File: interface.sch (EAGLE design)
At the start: 23 parts, among them U1 ISL3179EIBZ, U2 ATMEGA328P

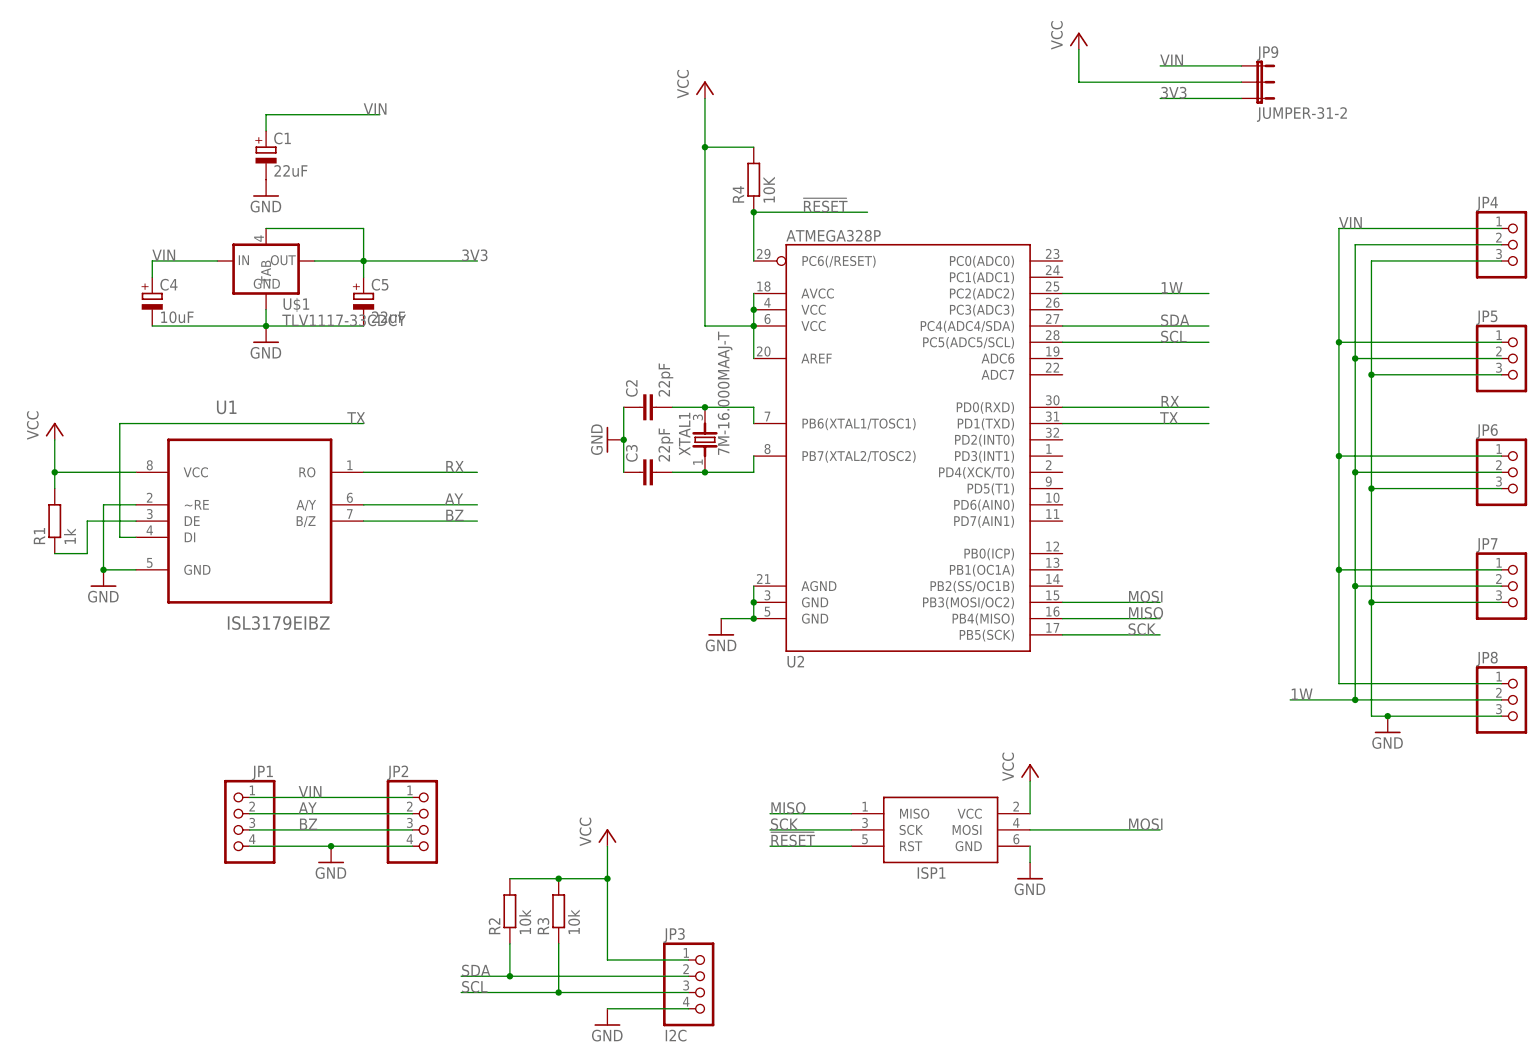
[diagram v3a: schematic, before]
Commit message: now has 2 I2C busses
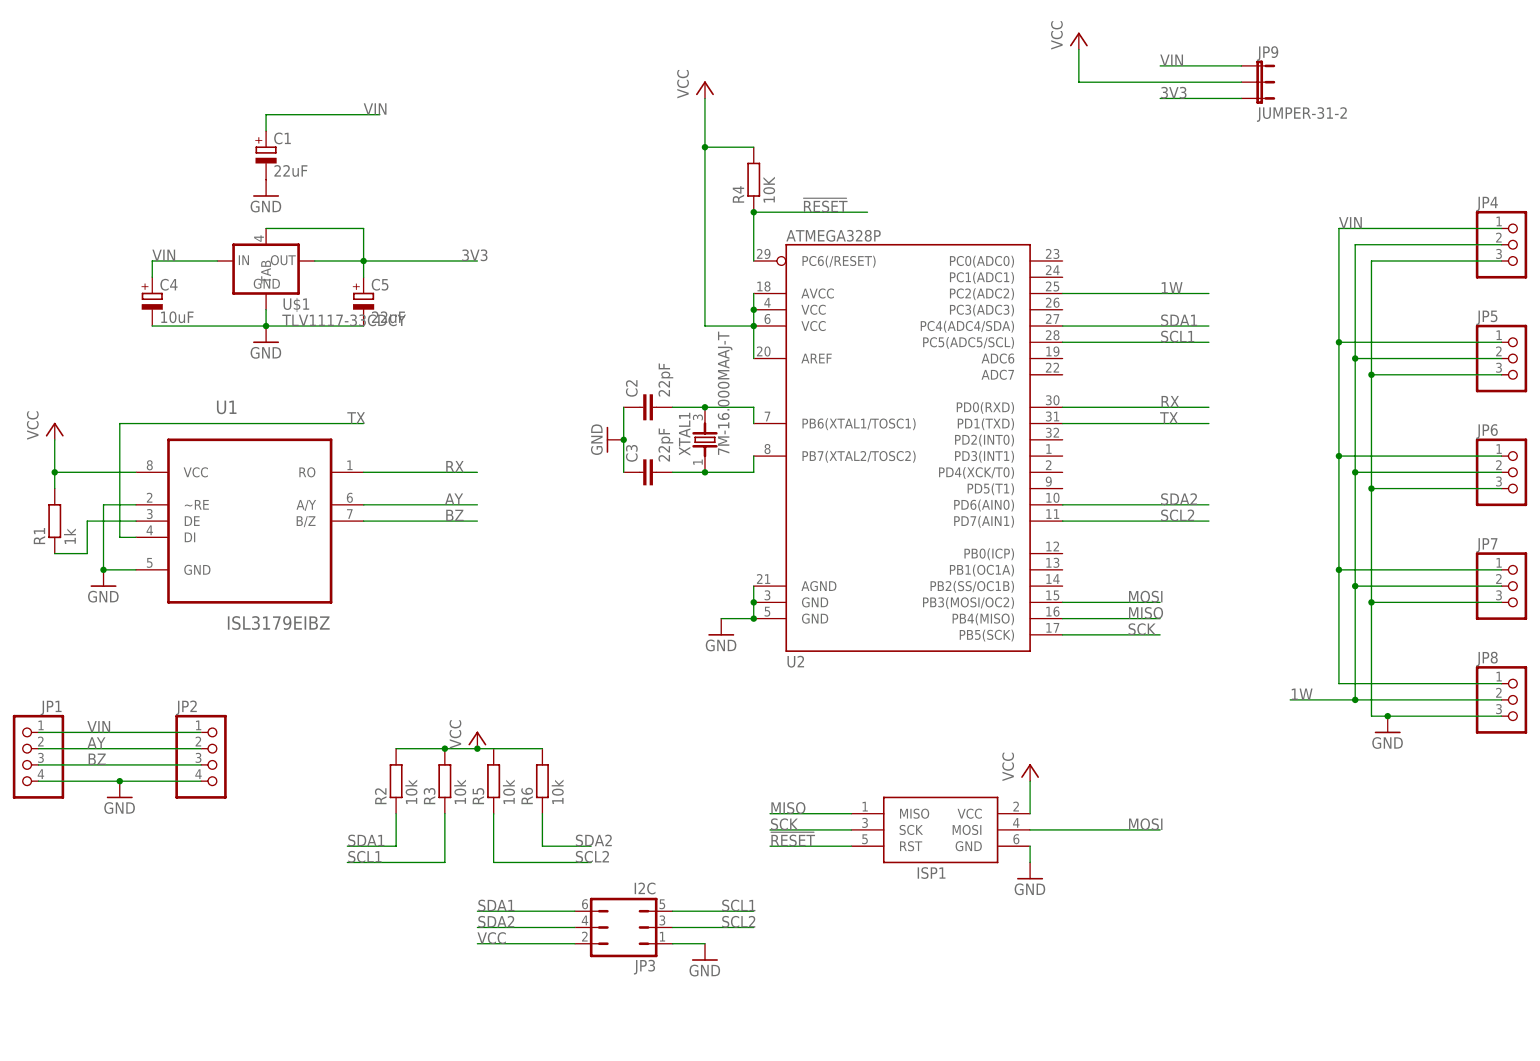
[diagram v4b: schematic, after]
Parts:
- added R5, R6: 10k, resistor:R-EU_R0805
- JP3: device pinhead:PINHD-1X4 -> jumper:JP3Q
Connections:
- removed net SCL: JP3.3, R3.1, U2.PC5(ADC5/SCL)
- removed net SDA: JP3.2, R2.1, U2.PC4(ADC4/SDA)
- new net SCL1: JP3.5, R3.1, U2.PC5(ADC5/SCL)
- new net SCL2: JP3.3, R5.1, U2.PD7(AIN1)
- new net SDA1: JP3.6, R2.1, U2.PC4(ADC4/SDA)
- new net SDA2: JP3.4, R6.1, U2.PD6(AIN0)
- net GND: now also JP3.1; no longer JP3.4
- net VCC: now also JP3.2, R5.2, R6.2; no longer JP3.1
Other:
- moved on the sheet: JP1, JP2, R2, R3
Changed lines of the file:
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@@
 <part name="GND1" library="supply1" deviceset="GND" device=""/>
 <part name="P+4" library="glacsweb" deviceset="VCC" device=""/>
-<part name="JP3" library="pinhead" deviceset="PINHD-1X4" device="" value="I2C"/>
+<part name="JP3" library="jumper" deviceset="JP3Q" device="" value="I2C"/>
 <part name="GND2" library="supply1" deviceset="GND" device=""/>
 <part name="P+6" library="glacsweb" deviceset="VCC" device=""/>
@@
 <part name="JP9" library="SparkFun-Passives" deviceset="JUMPER-3" device="1-2"/>
 <part name="P+5" library="glacsweb" deviceset="VCC" device=""/>
+<part name="R5" library="resistor" deviceset="R-EU_" device="R0805" value="10k"/>
+<part name="R6" library="resistor" deviceset="R-EU_" device="R0805" value="10k"/>
 </parts>
 <sheets>
@@
 <instance part="P+2" gate="VCC" x="165.1" y="53.34"/>
 <instance part="GND5" gate="1" x="165.1" y="35.56"/>
-<instance part="JP2" gate="A" x="71.12" y="43.18"/>
-<instance part="JP1" gate="A" x="40.64" y="43.18" rot="MR0"/>
-<instance part="GND6" gate="1" x="55.88" y="38.1"/>
+<instance part="JP2" gate="A" x="38.1" y="53.34"/>
+<instance part="JP1" gate="A" x="7.62" y="53.34" rot="MR0"/>
+<instance part="GND6" gate="1" x="22.86" y="48.26"/>
 <instance part="GND1" gate="1" x="45.72" y="142.24"/>
 <instance part="P+4" gate="VCC" x="12.7" y="106.68"/>
-<instance part="JP3" gate="A" x="114.3" y="17.78"/>
-<instance part="GND2" gate="1" x="99.06" y="12.7"/>
-<instance part="P+6" gate="VCC" x="99.06" y="43.18"/>
+<instance part="JP3" gate="B" x="101.6" y="27.94" rot="R90"/>
+<instance part="GND2" gate="1" x="114.3" y="22.86"/>
+<instance part="P+6" gate="VCC" x="78.74" y="58.42"/>
 <instance part="JP4" gate="A" x="241.3" y="134.62"/>
 <instance part="JP5" gate="A" x="241.3" y="116.84"/>
@@
 <instance part="JP8" gate="A" x="241.3" y="63.5"/>
 <instance part="GND7" gate="1" x="220.98" y="58.42"/>
-<instance part="R3" gate="G$1" x="91.44" y="30.48" rot="R90"/>
-<instance part="R2" gate="G$1" x="83.82" y="30.48" rot="R90"/>
+<instance part="R3" gate="G$1" x="73.66" y="50.8" rot="R90"/>
+<instance part="R2" gate="G$1" x="66.04" y="50.8" rot="R90"/>
 <instance part="U2" gate="G$1" x="144.78" y="106.68"/>
 <instance part="GND8" gate="1" x="116.84" y="73.66"/>
@@
 <instance part="JP9" gate="G$1" x="200.66" y="162.56" rot="R270"/>
 <instance part="P+5" gate="VCC" x="172.72" y="167.64"/>
+<instance part="R5" gate="G$1" x="81.28" y="50.8" rot="R90"/>
+<instance part="R6" gate="G$1" x="88.9" y="50.8" rot="R90"/>
 </instances>
 <busses>
@@
 <pinref part="JP1" gate="A" pin="4"/>
 <pinref part="JP2" gate="A" pin="4"/>
-<wire x1="43.18" y1="40.64" x2="55.88" y2="40.64" width="0.1524" layer="91"/>
+<wire x1="10.16" y1="50.8" x2="22.86" y2="50.8" width="0.1524" layer="91"/>
 <pinref part="GND6" gate="1" pin="GND"/>
-<wire x1="55.88" y1="40.64" x2="68.58" y2="40.64" width="0.1524" layer="91"/>
-<junction x="55.88" y="40.64"/>
+<wire x1="22.86" y1="50.8" x2="35.56" y2="50.8" width="0.1524" layer="91"/>
+<junction x="22.86" y="50.8"/>
 </segment>
 <segment>
 <pinref part="C1" gate="G$1" pin="-"/>
 <pinref part="GND1" gate="1" pin="GND"/>
-</segment>
-<segment>
-<pinref part="JP3" gate="A" pin="4"/>
-<pinref part="GND2" gate="1" pin="GND"/>
-<wire x1="111.76" y1="15.24" x2="99.06" y2="15.24" width="0.1524" layer="91"/>
 </segment>
 <segment>
@@
 <pinref part="GND9" gate="1" pin="GND"/>
 </segment>
+<segment>
+<pinref part="JP3" gate="B" pin="1"/>
+<pinref part="GND2" gate="1" pin="GND"/>
+<wire x1="109.22" y1="25.4" x2="114.3" y2="25.4" width="0.1524" layer="91"/>
+</segment>
 </net>
 <net name="VCC" class="0">
@@
 <wire x1="12.7" y1="96.52" x2="12.7" y2="99.06" width="0.1524" layer="91"/>
 <junction x="12.7" y="99.06"/>
-</segment>
-<segment>
-<pinref part="JP3" gate="A" pin="1"/>
-<pinref part="P+6" gate="VCC" pin="VCC"/>
-<wire x1="111.76" y1="22.86" x2="99.06" y2="22.86" width="0.1524" layer="91"/>
-<wire x1="99.06" y1="22.86" x2="99.06" y2="35.56" width="0.1524" layer="91"/>
-<pinref part="R2" gate="G$1" pin="2"/>
-<wire x1="99.06" y1="35.56" x2="99.06" y2="40.64" width="0.1524" layer="91"/>
-<wire x1="83.82" y1="35.56" x2="91.44" y2="35.56" width="0.1524" layer="91"/>
-<pinref part="R3" gate="G$1" pin="2"/>
-<junction x="91.44" y="35.56"/>
-<wire x1="91.44" y1="35.56" x2="99.06" y2="35.56" width="0.1524" layer="91"/>
-<junction x="99.06" y="35.56"/>
 </segment>
 <segment>
@@
 <pinref part="P+5" gate="VCC" pin="VCC"/>
 </segment>
+<segment>
+<pinref part="JP3" gate="B" pin="2"/>
+<wire x1="93.98" y1="25.4" x2="78.74" y2="25.4" width="0.1524" layer="91"/>
+<label x="78.74" y="25.4" size="1.778" layer="95"/>
+</segment>
+<segment>
+<pinref part="R2" gate="G$1" pin="2"/>
+<wire x1="66.04" y1="55.88" x2="73.66" y2="55.88" width="0.1524" layer="91"/>
+<pinref part="R3" gate="G$1" pin="2"/>
+<junction x="73.66" y="55.88"/>
+<wire x1="73.66" y1="55.88" x2="78.74" y2="55.88" width="0.1524" layer="91"/>
+<pinref part="R5" gate="G$1" pin="2"/>
+<pinref part="R6" gate="G$1" pin="2"/>
+<wire x1="78.74" y1="55.88" x2="81.28" y2="55.88" width="0.1524" layer="91"/>
+<wire x1="88.9" y1="55.88" x2="81.28" y2="55.88" width="0.1524" layer="91"/>
+<pinref part="P+6" gate="VCC" pin="VCC"/>
+<junction x="78.74" y="55.88"/>
+</segment>
 </net>
 <net name="AY" class="0">
@@
 <pinref part="JP2" gate="A" pin="2"/>
 <pinref part="JP1" gate="A" pin="2"/>
-<wire x1="68.58" y1="45.72" x2="43.18" y2="45.72" width="0.1524" layer="91"/>
-<label x="50.8" y="45.72" size="1.778" layer="95"/>
+<wire x1="35.56" y1="55.88" x2="10.16" y2="55.88" width="0.1524" layer="91"/>
+<label x="17.78" y="55.88" size="1.778" layer="95"/>
 </segment>
 </net>
@@
 <pinref part="JP1" gate="A" pin="3"/>
 <pinref part="JP2" gate="A" pin="3"/>
-<wire x1="43.18" y1="43.18" x2="68.58" y2="43.18" width="0.1524" layer="91"/>
-<label x="50.8" y="43.18" size="1.778" layer="95"/>
+<wire x1="10.16" y1="53.34" x2="35.56" y2="53.34" width="0.1524" layer="91"/>
+<label x="17.78" y="53.34" size="1.778" layer="95"/>
 </segment>
 </net>
@@
 </segment>
 </net>
-<net name="SDA" class="0">
-<segment>
-<pinref part="JP3" gate="A" pin="2"/>
-<wire x1="111.76" y1="20.32" x2="83.82" y2="20.32" width="0.1524" layer="91"/>
-<label x="76.2" y="20.32" size="1.778" layer="95"/>
+<net name="SDA1" class="0">
+<segment>
+<label x="58.42" y="40.64" size="1.778" layer="95"/>
 <pinref part="R2" gate="G$1" pin="1"/>
-<wire x1="83.82" y1="20.32" x2="76.2" y2="20.32" width="0.1524" layer="91"/>
-<wire x1="83.82" y1="25.4" x2="83.82" y2="20.32" width="0.1524" layer="91"/>
-<junction x="83.82" y="20.32"/>
+<wire x1="66.04" y1="40.64" x2="58.42" y2="40.64" width="0.1524" layer="91"/>
+<wire x1="66.04" y1="45.72" x2="66.04" y2="40.64" width="0.1524" layer="91"/>
 </segment>
 <segment>
@@
 <label x="185.42" y="121.92" size="1.778" layer="95"/>
 </segment>
-</net>
-<net name="SCL" class="0">
-<segment>
-<pinref part="JP3" gate="A" pin="3"/>
-<wire x1="111.76" y1="17.78" x2="91.44" y2="17.78" width="0.1524" layer="91"/>
-<label x="76.2" y="17.78" size="1.778" layer="95"/>
+<segment>
+<pinref part="JP3" gate="B" pin="6"/>
+<wire x1="93.98" y1="30.48" x2="78.74" y2="30.48" width="0.1524" layer="91"/>
+<label x="78.74" y="30.48" size="1.778" layer="95"/>
+</segment>
+</net>
+<net name="SCL1" class="0">
+<segment>
+<label x="58.42" y="38.1" size="1.778" layer="95"/>
 <pinref part="R3" gate="G$1" pin="1"/>
-<wire x1="91.44" y1="17.78" x2="76.2" y2="17.78" width="0.1524" layer="91"/>
-<wire x1="91.44" y1="25.4" x2="91.44" y2="17.78" width="0.1524" layer="91"/>
-<junction x="91.44" y="17.78"/>
+<wire x1="73.66" y1="38.1" x2="58.42" y2="38.1" width="0.1524" layer="91"/>
+<wire x1="73.66" y1="45.72" x2="73.66" y2="38.1" width="0.1524" layer="91"/>
 </segment>
 <segment>
@@
 <wire x1="170.18" y1="119.38" x2="193.04" y2="119.38" width="0.1524" layer="91"/>
 <label x="185.42" y="119.38" size="1.778" layer="95"/>
+</segment>
+<segment>
+<pinref part="JP3" gate="B" pin="5"/>
+<wire x1="109.22" y1="30.48" x2="121.92" y2="30.48" width="0.1524" layer="91"/>
+<label x="116.84" y="30.48" size="1.778" layer="95"/>
 </segment>
 </net>
@@
 <pinref part="JP1" gate="A" pin="1"/>
 <pinref part="JP2" gate="A" pin="1"/>
-<wire x1="43.18" y1="48.26" x2="68.58" y2="48.26" width="0.1524" layer="91"/>
-<label x="50.8" y="48.26" size="1.778" layer="95"/>
+<wire x1="10.16" y1="58.42" x2="35.56" y2="58.42" width="0.1524" layer="91"/>
+<label x="17.78" y="58.42" size="1.778" layer="95"/>
 </segment>
 <segment>
@@
 </segment>
 </net>
+<net name="SDA2" class="0">
+<segment>
+<pinref part="U2" gate="G$1" pin="PD6(AIN0)"/>
+<wire x1="170.18" y1="93.98" x2="193.04" y2="93.98" width="0.1524" layer="91"/>
+<label x="185.42" y="93.98" size="1.778" layer="95"/>
+</segment>
+<segment>
+<pinref part="R6" gate="G$1" pin="1"/>
+<wire x1="88.9" y1="45.72" x2="88.9" y2="40.64" width="0.1524" layer="91"/>
+<wire x1="88.9" y1="40.64" x2="96.52" y2="40.64" width="0.1524" layer="91"/>
+<label x="93.98" y="40.64" size="1.778" layer="95"/>
+</segment>
+<segment>
+<pinref part="JP3" gate="B" pin="4"/>
+<wire x1="93.98" y1="27.94" x2="78.74" y2="27.94" width="0.1524" layer="91"/>
+<label x="78.74" y="27.94" size="1.778" layer="95"/>
+</segment>
+</net>
+<net name="SCL2" class="0">
+<segment>
+<pinref part="U2" gate="G$1" pin="PD7(AIN1)"/>
+<wire x1="170.18" y1="91.44" x2="193.04" y2="91.44" width="0.1524" layer="91"/>
+<label x="185.42" y="91.44" size="1.778" layer="95"/>
+</segment>
+<segment>
+<pinref part="R5" gate="G$1" pin="1"/>
+<wire x1="81.28" y1="45.72" x2="81.28" y2="38.1" width="0.1524" layer="91"/>
+<wire x1="81.28" y1="38.1" x2="96.52" y2="38.1" width="0.1524" layer="91"/>
+<label x="93.98" y="38.1" size="1.778" layer="95"/>
+</segment>
+<segment>
+<pinref part="JP3" gate="B" pin="3"/>
+<wire x1="109.22" y1="27.94" x2="121.92" y2="27.94" width="0.1524" layer="91"/>
+<label x="116.84" y="27.94" size="1.778" layer="95"/>
+</segment>
+</net>

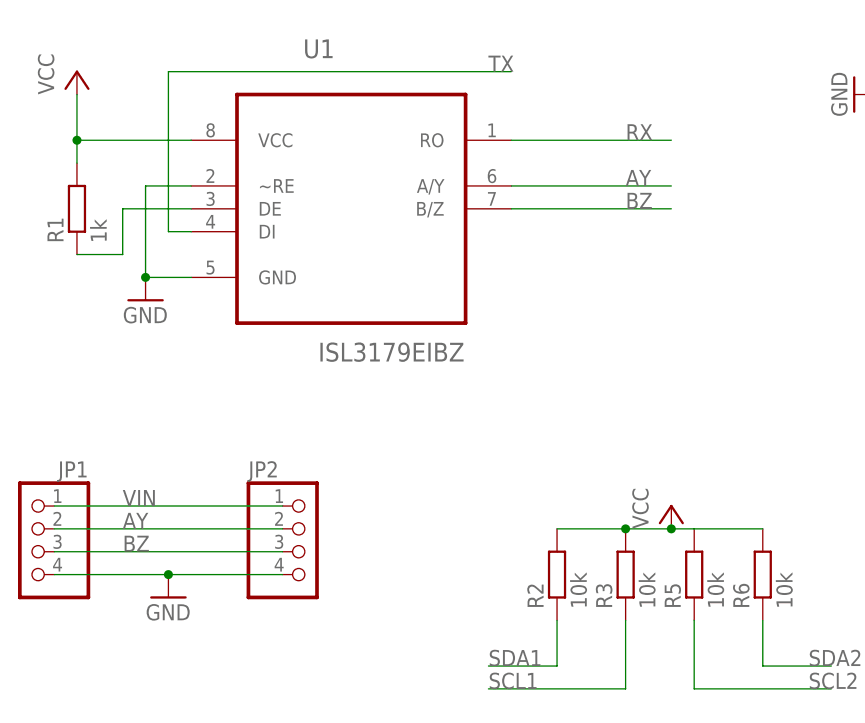
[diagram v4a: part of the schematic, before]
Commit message: track lengths now within 0.2% for rs485
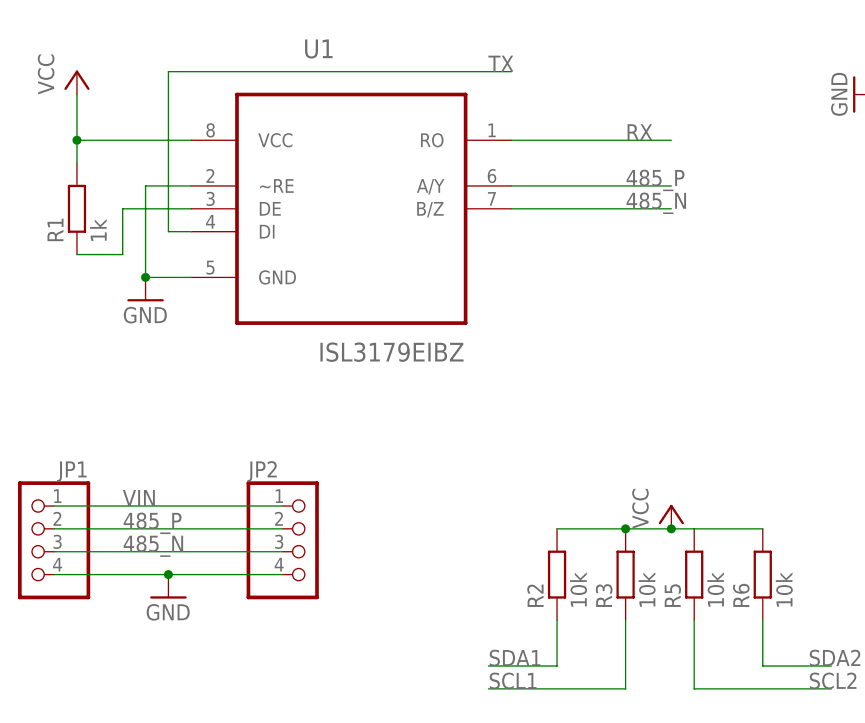
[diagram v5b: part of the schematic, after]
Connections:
- net AY renamed 485_P
- net BZ renamed 485_N
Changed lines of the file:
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@@
 <?xml version="1.0" encoding="utf-8"?>
 <!DOCTYPE eagle SYSTEM "eagle.dtd">
-<eagle version="6.5.0">
+<eagle version="6.6.0">
 <drawing>
 <settings>
@@
 <class number="0" name="default" width="0" drill="0">
 </class>
+<class number="1" name="rs485" width="0.3048" drill="0">
+<clearance class="1" value="0.1524"/>
+</class>
 </classes>
 <parts>
@@
 </segment>
 </net>
-<net name="AY" class="0">
-<segment>
-<pinref part="U1" gate="A" pin="A/Y"/>
-<wire x1="60.96" y1="93.98" x2="78.74" y2="93.98" width="0.1524" layer="91"/>
-<label x="73.66" y="93.98" size="1.778" layer="95"/>
-</segment>
-<segment>
-<pinref part="JP2" gate="A" pin="2"/>
-<pinref part="JP1" gate="A" pin="2"/>
-<wire x1="35.56" y1="55.88" x2="10.16" y2="55.88" width="0.1524" layer="91"/>
-<label x="17.78" y="55.88" size="1.778" layer="95"/>
-</segment>
-</net>
-<net name="BZ" class="0">
+<net name="485_N" class="1">
 <segment>
 <pinref part="U1" gate="A" pin="B/Z"/>
@@
 </segment>
 </net>
+<net name="485_P" class="1">
+<segment>
+<pinref part="U1" gate="A" pin="A/Y"/>
+<wire x1="60.96" y1="93.98" x2="78.74" y2="93.98" width="0.1524" layer="91"/>
+<label x="73.66" y="93.98" size="1.778" layer="95"/>
+</segment>
+<segment>
+<pinref part="JP2" gate="A" pin="2"/>
+<pinref part="JP1" gate="A" pin="2"/>
+<wire x1="35.56" y1="55.88" x2="10.16" y2="55.88" width="0.1524" layer="91"/>
+<label x="17.78" y="55.88" size="1.778" layer="95"/>
+</segment>
+</net>
